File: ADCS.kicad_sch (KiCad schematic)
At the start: 14 parts

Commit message: Interboard added
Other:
- sheet Interboard ports: added 12V, 5V, I2C_SCL_3V3, I2C_SDA_3V3; removed none
- sheet Power ports: added 12V, 5V; removed none

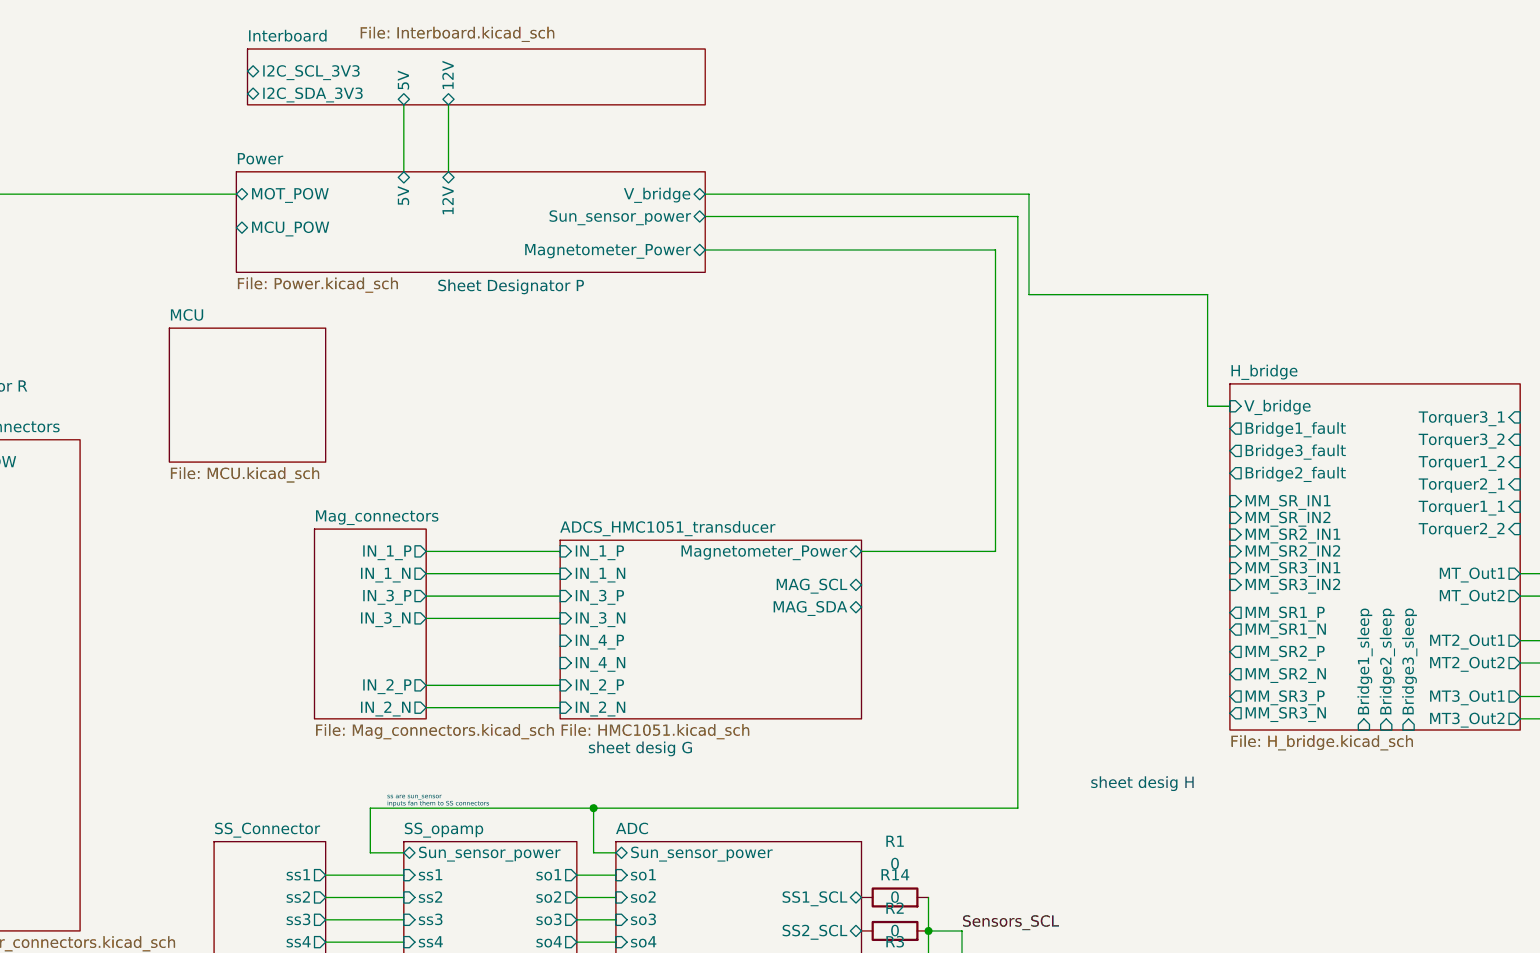
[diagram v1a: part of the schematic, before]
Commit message: all sheet designators added
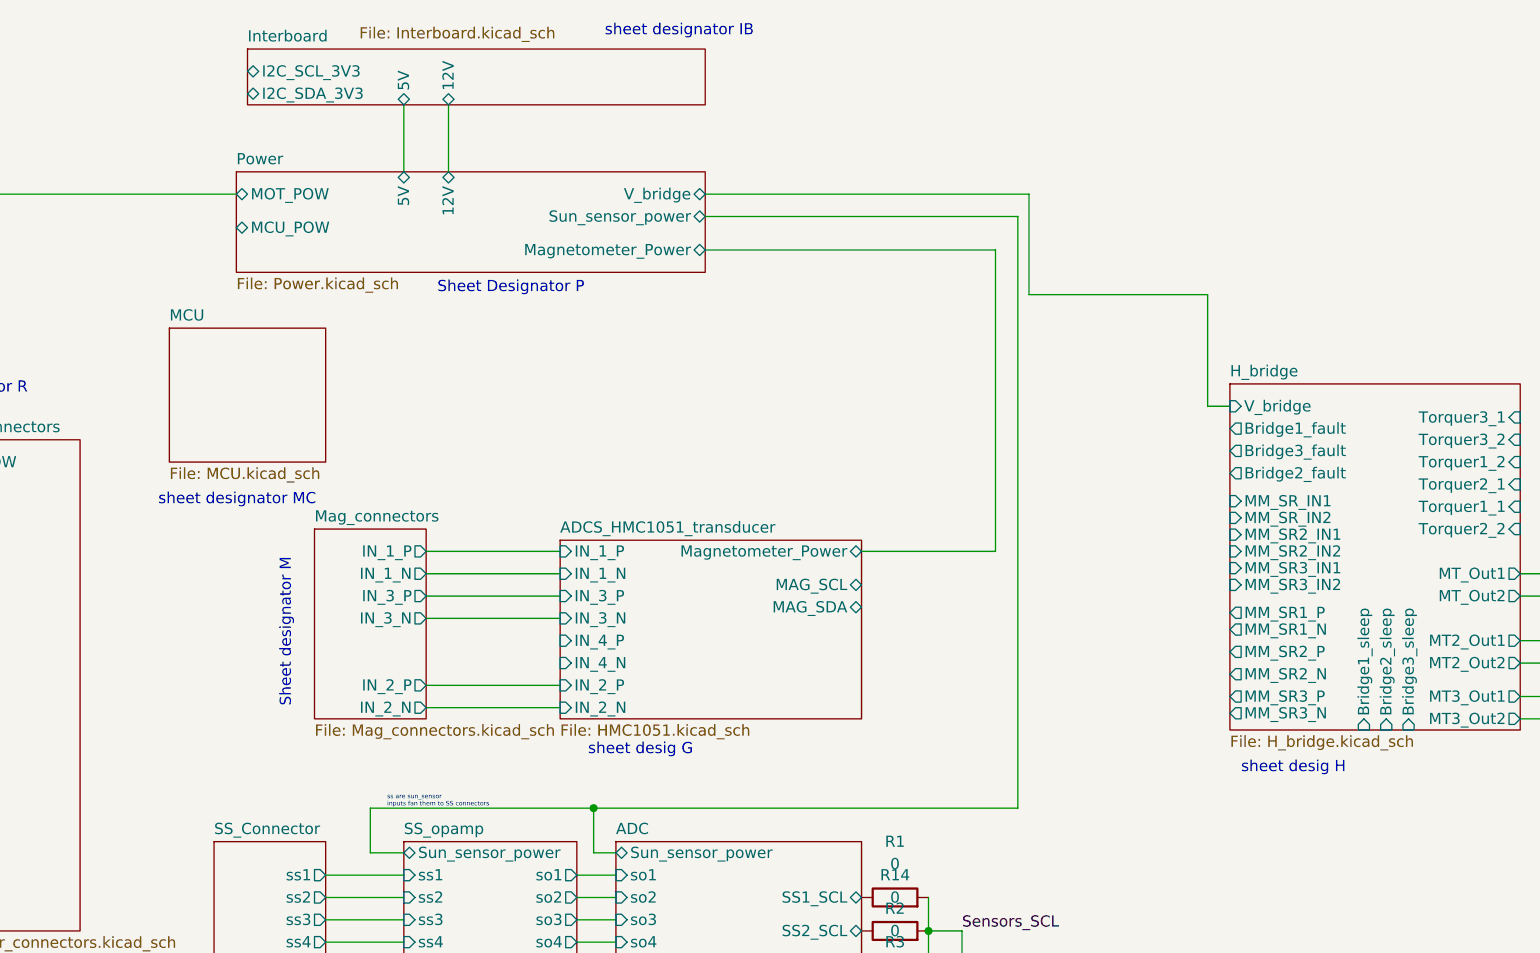
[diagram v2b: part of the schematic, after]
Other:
- note added: "Sheet designator M"
- note added: "sheet designator IB"
- note added: "sheet designator MC"
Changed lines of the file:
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@@
     (effects (font (size 0.508 0.508)) (justify left bottom))
+  )
+  (text "Sheet designator M\n" (at 110.49 91.44 90)
+    (effects (font (size 1.27 1.27)) (justify left bottom))
   )
   (text "Sheet desig : A\n\n" (at 29.21 76.2 0)
@@
     (effects (font (size 1.27 1.27)) (justify left bottom))
   )
+  (text "sheet designator IB \n" (at 146.05 15.24 0)
+    (effects (font (size 1.27 1.27)) (justify left bottom))
+  )
   (text "sheet desig G\n\n" (at 144.145 99.06 0)
+    (effects (font (size 1.27 1.27)) (justify left bottom))
+  )
+  (text "sheet designator MC\n" (at 95.25 68.58 0)
     (effects (font (size 1.27 1.27)) (justify left bottom))
   )
@@
     (effects (font (size 1.27 1.27) (thickness 0.254) bold) (justify left bottom))
   )
-  (text "sheet desig H\n" (at 201.295 100.965 0)
+  (text "sheet desig H\n" (at 218.44 99.06 0)
     (effects (font (size 1.27 1.27)) (justify left bottom))
   )
@@
       (reference "J1") (unit 1) (value "Conn_ARM_JTAG_SWD_10") (footprint "")
     )
-    (path "/90eea1cc-3897-47cb-b6ba-95228c17b7e0/4258d828-95d7-4ac0-9c18-738f3bf4ca4e"
-      (reference "JB1") (unit 1) (value "502352-0210") (footprint "")
-    )
-    (path "/90eea1cc-3897-47cb-b6ba-95228c17b7e0/85986521-380c-46b6-84df-2f18d65ade2d"
-      (reference "JB2") (unit 1) (value "502352-0210") (footprint "")
-    )
-    (path "/90eea1cc-3897-47cb-b6ba-95228c17b7e0/751c002d-c9ed-4f6f-bf56-77d36fe6f8f9"
-      (reference "JB3") (unit 1) (value "502352-0210") (footprint "")
-    )
     (path "/8fa611b7-cf75-4378-bd5d-72096b0e3078/97355b07-3b0f-4286-b37c-a4c08e6a759a"
       (reference "JIB") (unit 1) (value "2367196-8") (footprint "")
     )
+    (path "/90eea1cc-3897-47cb-b6ba-95228c17b7e0/4258d828-95d7-4ac0-9c18-738f3bf4ca4e"
+      (reference "JM1") (unit 1) (value "502352-0210") (footprint "")
+    )
+    (path "/90eea1cc-3897-47cb-b6ba-95228c17b7e0/85986521-380c-46b6-84df-2f18d65ade2d"
+      (reference "JM2") (unit 1) (value "502352-0210") (footprint "")
+    )
+    (path "/90eea1cc-3897-47cb-b6ba-95228c17b7e0/751c002d-c9ed-4f6f-bf56-77d36fe6f8f9"
+      (reference "JM3") (unit 1) (value "502352-0210") (footprint "")
+    )
     (path "/7a353e73-f362-4813-b2c3-9e73ce7ee8de/c0b6aae2-d2fb-4c24-8018-c87793aa0bc5"

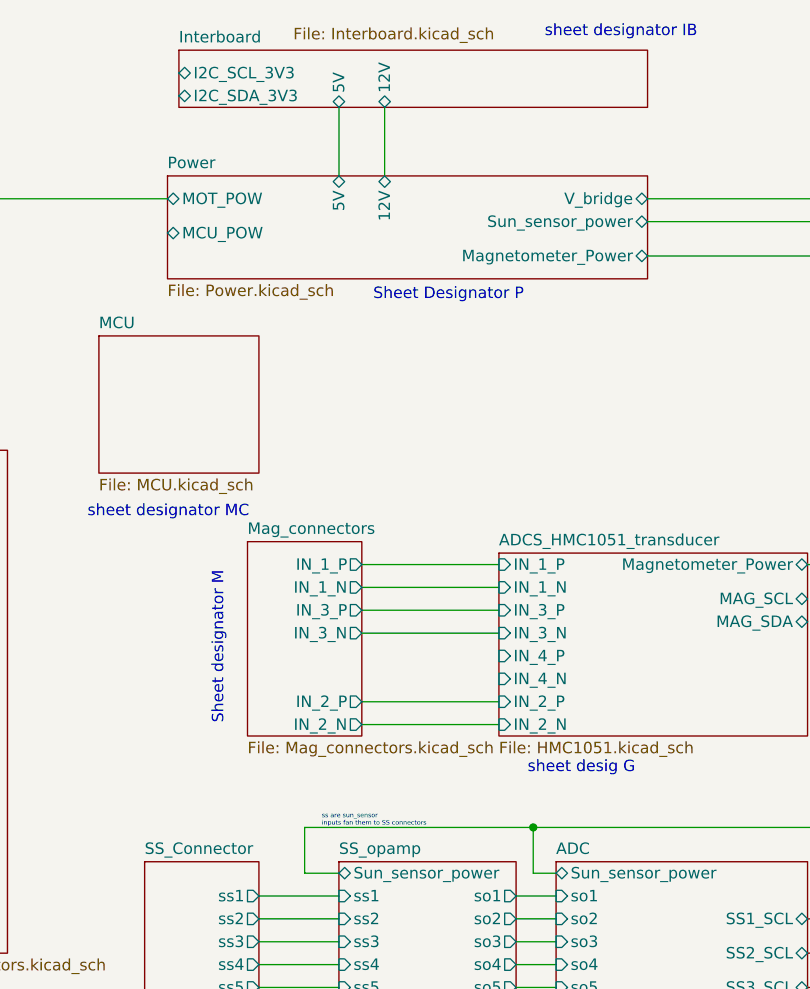
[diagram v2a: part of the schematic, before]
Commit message: Reset switch added
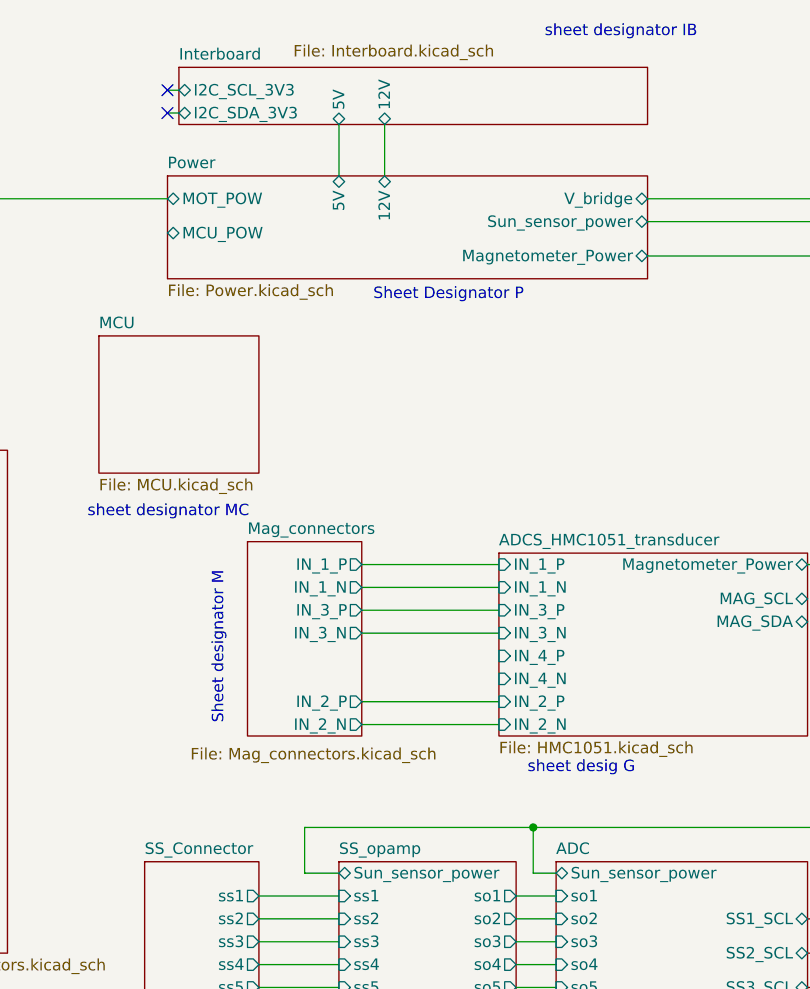
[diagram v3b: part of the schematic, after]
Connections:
- no-connect marks 0 -> 2
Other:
- note removed: "ss are sun_sensor inputs fan them to SS connectors"
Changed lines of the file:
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@@
   (junction (at 182.88 124.46) (diameter 0) (color 0 0 0 0)
   )
+  (no_connect (at 104.14 20.955))
+  (no_connect (at 104.14 23.495))
   (wire (pts (xy 29.21 111.76) (xy 25.4 111.76))
     (stroke (width 0) (type default) (color 0 0 0 0))
@@
     (stroke (width 0) (type default) (color 0 0 0 0))
   )
+  (wire (pts (xy 104.14 23.495) (xy 105.41 23.495))
+    (stroke (width 0) (type default) (color 0 0 0 0))
+  )
   (wire (pts (xy 66.04 33.02) (xy 66.04 63.5))
     (stroke (width 0) (type default) (color 0 0 0 0))
@@
     (stroke (width 0) (type default) (color 0 0 0 0))
   )
+  (wire (pts (xy 104.14 20.955) (xy 105.41 20.955))
+    (stroke (width 0) (type default) (color 0 0 0 0))
+  )
   (wire (pts (xy 25.4 80.01) (xy 25.4 48.26))
     (stroke (width 0) (type default) (color 0 0 0 0))
@@
     (stroke (width 0) (type default) (color 0 0 0 0))
   )
-  (wire (pts (xy 128.27 22.86) (xy 128.27 30.48))
+  (wire (pts (xy 128.27 24.765) (xy 128.27 30.48))
     (stroke (width 0) (type default) (color 0 0 0 0))
   )
@@
     (stroke (width 0) (type default) (color 0 0 0 0))
   )
-  (wire (pts (xy 123.19 22.86) (xy 123.19 30.48))
+  (wire (pts (xy 123.19 24.765) (xy 123.19 30.48))
     (stroke (width 0) (type default) (color 0 0 0 0))
   )
   (wire (pts (xy 54.61 80.01) (xy 54.61 81.28))
     (stroke (width 0) (type default) (color 0 0 0 0))
-  )
-  (text "ss are sun_sensor \ninputs fan them to SS connectors\n"
-    (at 121.285 102.87 0)
-    (effects (font (size 0.508 0.508)) (justify left bottom))
   )
   (text "Sheet designator M\n" (at 110.49 91.44 90)
@@
     )
   )
-  (sheet (at 105.41 16.51) (size 52.07 6.35)
+  (sheet (at 105.41 18.415) (size 52.07 6.35)
     (stroke (width 0.1524) (type solid) (color 0 0 0 0))
     (fill (color 0 0 0 0.0000))
-    (property "Sheet name" "Interboard" (id 0) (at 105.41 15.7984 0)
+    (property "Sheet name" "Interboard" (id 0) (at 105.41 17.7034 0)
       (effects (font (size 1.27 1.27)) (justify left bottom))
     )
-    (property "Sheet file" "Interboard.kicad_sch" (id 1) (at 118.11 13.97 0)
+    (property "Sheet file" "Interboard.kicad_sch" (id 1) (at 118.11 15.875 0)
       (effects (font (size 1.27 1.27)) (justify left top))
     )
-    (pin "5V" bidirectional (at 123.19 22.86 270)
-      (effects (font (size 1.27 1.27)) (justify left))
-    )
-    (pin "12V" bidirectional (at 128.27 22.86 270)
-      (effects (font (size 1.27 1.27)) (justify left))
-    )
-    (pin "I2C_SDA_3V3" bidirectional (at 105.41 21.59 180)
-      (effects (font (size 1.27 1.27)) (justify left))
-    )
-    (pin "I2C_SCL_3V3" bidirectional (at 105.41 19.05 180)
-      (effects (font (size 1.27 1.27)) (justify left))
-    )
-  )
-  (sheet (at 113.03 71.12) (size 12.7 21.59) (fields_autoplaced)
+    (pin "5V" bidirectional (at 123.19 24.765 270)
+      (effects (font (size 1.27 1.27)) (justify left))
+    )
+    (pin "12V" bidirectional (at 128.27 24.765 270)
+      (effects (font (size 1.27 1.27)) (justify left))
+    )
+    (pin "I2C_SDA_3V3" bidirectional (at 105.41 23.495 180)
+      (effects (font (size 1.27 1.27)) (justify left))
+    )
+    (pin "I2C_SCL_3V3" bidirectional (at 105.41 20.955 180)
+      (effects (font (size 1.27 1.27)) (justify left))
+    )
+  )
+  (sheet (at 113.03 71.12) (size 12.7 21.59)
     (stroke (width 0.1524) (type solid) (color 0 0 0 0))
     (fill (color 173 230 255 1.0000))
@@
       (effects (font (size 1.27 1.27)) (justify left bottom))
     )
-    (property "Sheet file" "Mag_connectors.kicad_sch" (id 1) (at 113.03 93.2946 0)
+    (property "Sheet file" "Mag_connectors.kicad_sch" (id 1) (at 106.68 93.98 0)
       (effects (font (size 1.27 1.27)) (justify left top))
     )
@@
       (reference "#PWR?") (unit 1) (value "GND") (footprint "")
     )
+    (path "/212d50e9-da32-4d3f-8d53-7380f45f0f28/2cf19562-a990-4d21-98af-16574ac3e108"
+      (reference "#PWR?") (unit 1) (value "GND") (footprint "")
+    )
     (path "/4c63012e-f7ed-4767-81b5-36fd3817b900/2d5c5ceb-06f5-4883-a5ec-e3e8242e2aba"
       (reference "#PWR?") (unit 1) (value "GND") (footprint "")
@@
       (reference "#PWR?") (unit 1) (value "GND") (footprint "")
     )
-    (path "/212d50e9-da32-4d3f-8d53-7380f45f0f28/fea6d1c0-dee6-47b2-b0b8-fa7833396fbd"
-      (reference "#PWR?") (unit 1) (value "GND") (footprint "")
-    )
     (path "/bada602b-dbd3-4fb8-afdd-ed6e71e7ad90/09e9f576-75ea-4b13-ba60-52e7e8cae27e"
       (reference "C?") (unit 1) (value "C") (footprint "")
@@
       (reference "JT3") (unit 1) (value "502352-0210") (footprint "")
     )
-    (path "/212d50e9-da32-4d3f-8d53-7380f45f0f28/7084612d-5a08-4e97-89ef-7cbc66cf7be0"
-      (reference "JTAG") (unit 1) (value "Conn_ARM_JTAG_SWD_20") (footprint "")
-    )
     (path "/fb0a46e4-ada8-472b-b73c-3a0177e61b01/d2b5f9be-c67e-4ed9-ab11-4136b7ba494f"
       (reference "LP1") (unit 1) (value "3.3u") (footprint "")
@@
       (reference "RP6") (unit 1) (value "62k") (footprint "")
     )
+    (path "/212d50e9-da32-4d3f-8d53-7380f45f0f28/6788fdae-820c-4646-bb86-ab490b0a25b9"
+      (reference "SW?") (unit 1) (value "SW_SPDT") (footprint "")
+    )
     (path "/85fce53c-db5d-41a5-af86-f02ad1af70e7/6c121213-a643-424f-99d1-9d43d03e252c"
